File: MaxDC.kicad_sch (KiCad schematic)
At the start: 32 parts, among them J1 Screw_Terminal_01x03, J2 Screw_Terminal_01x04, T2 70063K

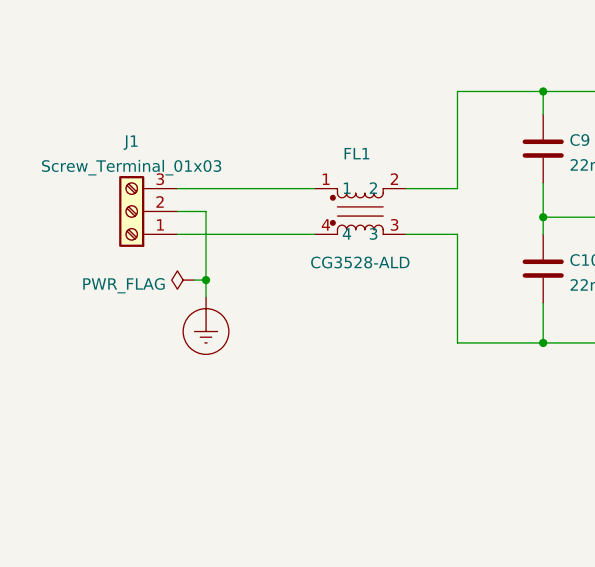
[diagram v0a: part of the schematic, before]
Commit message: Add files via upload
Begin Changes for creepage.   Reverse N and E input terminals.
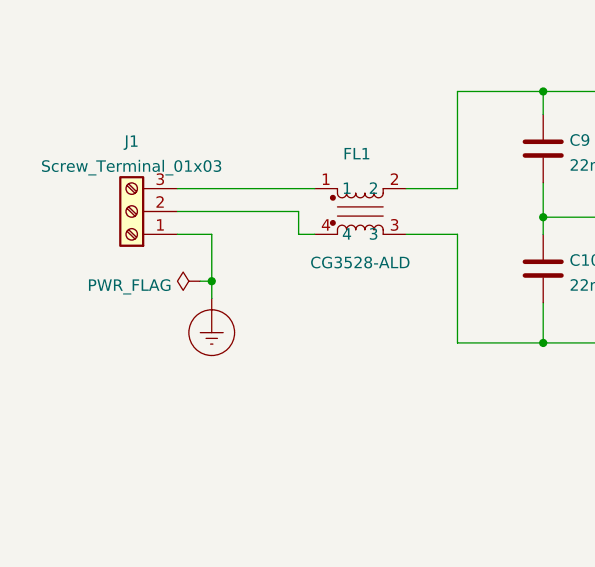
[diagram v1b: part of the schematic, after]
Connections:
- net Earth_Protective: now also J1.1 (Pin_1); no longer J1.2 (Pin_2)
- net at FL1.4: now also J1.2 (Pin_2); no longer J1.1 (Pin_1)
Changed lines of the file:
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@@
   (junction (at 164.465 110.49) (diameter 0) (color 0 0 0 0)
   )
-  (junction (at 45.085 92.71) (diameter 0) (color 0 0 0 0)
-  )
   (junction (at 134.62 110.49) (diameter 0) (color 0 0 0 0)
   )
@@
   (junction (at 82.55 85.725) (diameter 0) (color 0 0 0 0)
   )
+  (junction (at 45.72 92.837) (diameter 0) (color 0 0 0 0)
+  )
   (junction (at 200.66 60.325) (diameter 0) (color 0 0 0 0)
   )
@@
     (stroke (width 0) (type default) (color 0 0 0 0))
   )
+  (wire (pts (xy 45.72 92.837) (xy 45.72 94.742))
+    (stroke (width 0) (type default) (color 0 0 0 0))
+  )
   (wire (pts (xy 130.81 41.275) (xy 130.81 43.815))
     (stroke (width 0) (type default) (color 0 0 0 0))
@@
     (stroke (width 0) (type default) (color 0 0 0 0))
   )
-  (wire (pts (xy 45.085 92.71) (xy 45.085 85.09))
-    (stroke (width 0) (type default) (color 0 0 0 0))
-  )
   (wire (pts (xy 245.745 67.945) (xy 251.46 67.945))
     (stroke (width 0) (type default) (color 0 0 0 0))
@@
     (stroke (width 0) (type default) (color 0 0 0 0))
   )
-  (wire (pts (xy 45.085 92.71) (xy 45.085 94.615))
+  (wire (pts (xy 55.372 87.63) (xy 57.15 87.63))
     (stroke (width 0) (type default) (color 0 0 0 0))
   )
@@
     (stroke (width 0) (type default) (color 0 0 0 0))
   )
+  (wire (pts (xy 41.91 87.63) (xy 45.72 87.63))
+    (stroke (width 0) (type default) (color 0 0 0 0))
+  )
   (wire (pts (xy 164.465 86.36) (xy 179.07 86.36))
     (stroke (width 0) (type default) (color 0 0 0 0))
@@
     (stroke (width 0) (type default) (color 0 0 0 0))
   )
-  (wire (pts (xy 41.91 85.09) (xy 45.085 85.09))
-    (stroke (width 0) (type default) (color 0 0 0 0))
-  )
   (wire (pts (xy 148.59 86.36) (xy 148.59 92.075))
     (stroke (width 0) (type default) (color 0 0 0 0))
@@
     (stroke (width 0) (type default) (color 0 0 0 0))
   )
+  (wire (pts (xy 41.91 85.09) (xy 55.372 85.09))
+    (stroke (width 0) (type default) (color 0 0 0 0))
+  )
   (wire (pts (xy 156.21 59.055) (xy 156.21 60.325))
     (stroke (width 0) (type default) (color 0 0 0 0))
@@
     (stroke (width 0) (type default) (color 0 0 0 0))
   )
+  (wire (pts (xy 55.372 85.09) (xy 55.372 87.63))
+    (stroke (width 0) (type default) (color 0 0 0 0))
+  )
   (wire (pts (xy 73.025 82.55) (xy 73.025 71.755))
     (stroke (width 0) (type default) (color 0 0 0 0))
@@
     (stroke (width 0) (type default) (color 0 0 0 0))
   )
+  (wire (pts (xy 45.72 87.63) (xy 45.72 92.837))
+    (stroke (width 0) (type default) (color 0 0 0 0))
+  )
   (wire (pts (xy 245.745 70.485) (xy 251.46 70.485))
     (stroke (width 0) (type default) (color 0 0 0 0))
@@
     (stroke (width 0) (type default) (color 0 0 0 0))
   )
-  (wire (pts (xy 41.91 87.63) (xy 57.15 87.63))
-    (stroke (width 0) (type default) (color 0 0 0 0))
-  )
-  (wire (pts (xy 43.815 92.71) (xy 45.085 92.71))
+  (wire (pts (xy 44.45 92.837) (xy 45.72 92.837))
     (stroke (width 0) (type default) (color 0 0 0 0))
   )
@@
     (pin "2")
   )
-  (symbol (lib_id "power:Earth_Protective") (at 45.085 94.615 0) (unit 1)
+  (symbol (lib_id "power:Earth_Protective") (at 45.72 94.742 0) (unit 1)
     (in_bom yes) (on_board yes) (fields_autoplaced)
-    (property "Reference" "#PWR0101" (id 0) (at 51.435 100.965 0)
-      (effects (font (size 1.27 1.27)) hide)
-    )
-    (property "Value" "Earth_Protective" (id 1) (at 56.515 98.425 0)
-      (effects (font (size 1.27 1.27)) hide)
-    )
-    (property "Footprint" "" (id 2) (at 45.085 97.155 0)
-      (effects (font (size 1.27 1.27)) hide)
-    )
-    (property "Datasheet" "~" (id 3) (at 45.085 97.155 0)
+    (property "Reference" "#PWR0101" (id 0) (at 52.07 101.092 0)
+      (effects (font (size 1.27 1.27)) hide)
+    )
+    (property "Value" "Earth_Protective" (id 1) (at 57.15 98.552 0)
+      (effects (font (size 1.27 1.27)) hide)
+    )
+    (property "Footprint" "" (id 2) (at 45.72 97.282 0)
+      (effects (font (size 1.27 1.27)) hide)
+    )
+    (property "Datasheet" "~" (id 3) (at 45.72 97.282 0)
       (effects (font (size 1.27 1.27)) hide)
     )
@@
     )
   )
-  (symbol (lib_id "power:PWR_FLAG") (at 43.815 92.71 90) (unit 1)
+  (symbol (lib_id "power:PWR_FLAG") (at 44.45 92.837 90) (unit 1)
     (in_bom yes) (on_board yes) (fields_autoplaced)
-    (property "Reference" "#FLG0101" (id 0) (at 41.91 92.71 0)
-      (effects (font (size 1.27 1.27)) hide)
-    )
-    (property "Value" "PWR_FLAG" (id 1) (at 40.6401 93.189 90)
+    (property "Reference" "#FLG0101" (id 0) (at 42.545 92.837 0)
+      (effects (font (size 1.27 1.27)) hide)
+    )
+    (property "Value" "PWR_FLAG" (id 1) (at 41.2751 93.316 90)
       (effects (font (size 1.27 1.27)) (justify left))
     )
-    (property "Footprint" "" (id 2) (at 43.815 92.71 0)
-      (effects (font (size 1.27 1.27)) hide)
-    )
-    (property "Datasheet" "~" (id 3) (at 43.815 92.71 0)
-      (effects (font (size 1.27 1.27)) hide)
-    )
+    (property "Footprint" "" (id 2) (at 44.45 92.837 0)
+      (effects (font (size 1.27 1.27)) hide)
+    )
+    (property "Datasheet" "~" (id 3) (at 44.45 92.837 0)
+      (effects (font (size 1.27 1.27)) hide)
+    )

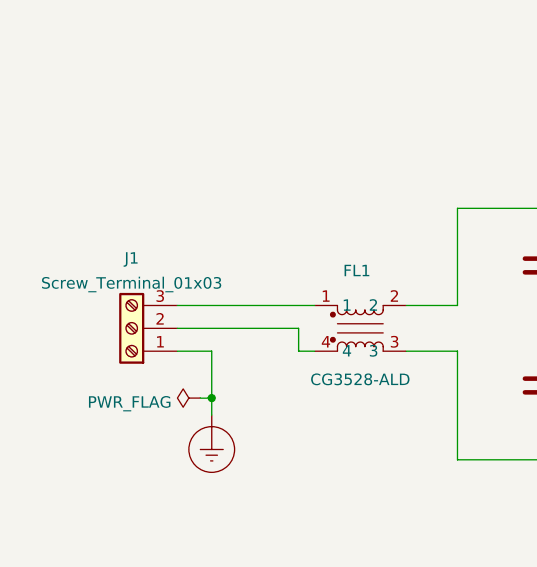
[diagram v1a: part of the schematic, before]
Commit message: Add files via upload
Adjust placement and spacing for 240VAC safety.   Slots not needed.
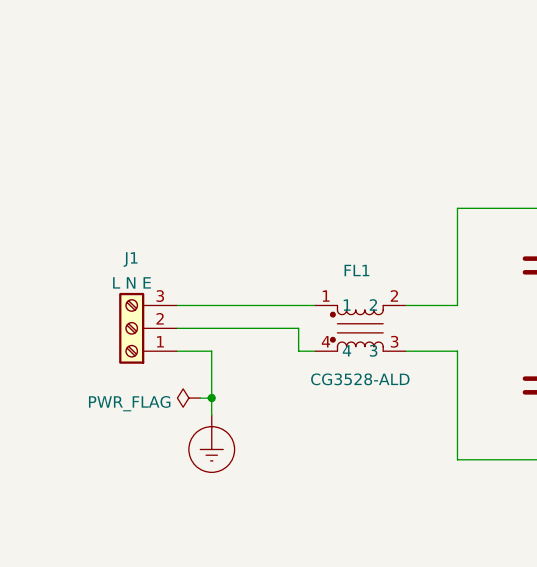
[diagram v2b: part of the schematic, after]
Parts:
- C10, C9: footprint Capacitor_THT:C_Rect_L18.0mm_W7.0mm_P15.00mm_FKS3_FKP3 -> Capacitor_THT:C_Rect_L18.0mm_W8.0mm_P15.00mm_FKS3_FKP3
- J1: value Screw_Terminal_01x03 -> L N E
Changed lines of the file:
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@@
   (title_block
     (title "MaxDC")
-    (date "2023-01-23")
+    (date "2023-01-24")
     (rev "0.2")
     (company "Author: Andrew Fischer\\nLicense: CC BY-NC 4.0 \\ncreativecommons.org/licenses/by-nc/4.0")
@@
     (in_bom yes) (on_board yes) (fields_autoplaced)
     (property "Reference" "J1" (id 0) (at 36.83 77.3135 0))
-    (property "Value" "Screw_Terminal_01x03" (id 1) (at 36.83 80.0886 0))
+    (property "Value" "L N E" (id 1) (at 36.83 80.0886 0))
     (property "Footprint" "TerminalBlock_Phoenix:TerminalBlock_Phoenix_MKDS-3-3-5.08_1x03_P5.08mm_Horizontal" (id 2) (at 36.83 85.09 0)
       (effects (font (size 1.27 1.27)) hide)
@@
       (effects (font (size 1.27 1.27)) (justify left))
     )
-    (property "Footprint" "Capacitor_THT:C_Rect_L18.0mm_W7.0mm_P15.00mm_FKS3_FKP3" (id 2) (at 83.5152 95.25 0)
+    (property "Footprint" "Capacitor_THT:C_Rect_L18.0mm_W8.0mm_P15.00mm_FKS3_FKP3" (id 2) (at 83.5152 95.25 0)
       (effects (font (size 1.27 1.27)) hide)
     )
@@
       (effects (font (size 1.27 1.27)) (justify left))
     )
-    (property "Footprint" "Capacitor_THT:C_Rect_L18.0mm_W7.0mm_P15.00mm_FKS3_FKP3" (id 2) (at 83.5152 81.915 0)
+    (property "Footprint" "Capacitor_THT:C_Rect_L18.0mm_W8.0mm_P15.00mm_FKS3_FKP3" (id 2) (at 83.5152 81.915 0)
       (effects (font (size 1.27 1.27)) hide)
     )
@@
     )
     (path "/f6f2e88a-815f-4070-b649-6d25db987473"
-      (reference "C9") (unit 1) (value "22nF") (footprint "Capacitor_THT:C_Rect_L18.0mm_W7.0mm_P15.00mm_FKS3_FKP3")
+      (reference "C9") (unit 1) (value "22nF") (footprint "Capacitor_THT:C_Rect_L18.0mm_W8.0mm_P15.00mm_FKS3_FKP3")
     )
     (path "/f46e4ec6-65a3-43ca-ba01-562772b6925d"
-      (reference "C10") (unit 1) (value "22nF") (footprint "Capacitor_THT:C_Rect_L18.0mm_W7.0mm_P15.00mm_FKS3_FKP3")
+      (reference "C10") (unit 1) (value "22nF") (footprint "Capacitor_THT:C_Rect_L18.0mm_W8.0mm_P15.00mm_FKS3_FKP3")
     )
     (path "/b1cd0cd8-a0ec-48c6-ae1d-c030f1e9f6c9"
@@
     )
     (path "/08e532fc-9580-46ad-af97-662135bee1de"
-      (reference "J1") (unit 1) (value "Screw_Terminal_01x03") (footprint "TerminalBlock_Phoenix:TerminalBlock_Phoenix_MKDS-3-3-5.08_1x03_P5.08mm_Horizontal")
+      (reference "J1") (unit 1) (value "L N E") (footprint "TerminalBlock_Phoenix:TerminalBlock_Phoenix_MKDS-3-3-5.08_1x03_P5.08mm_Horizontal")
     )
     (path "/c9494eea-a92e-41ee-83d6-7fde7a0d0d70"

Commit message: Add files via upload
28012023 Uploaded to JLCPCB
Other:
- note added: "C9 and C10 must be class Y."
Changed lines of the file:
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@@
   (title_block
     (title "MaxDC")
-    (date "2023-01-24")
-    (rev "0.2")
+    (date "2023-01-28")
+    (rev "0.3")
     (company "Author: Andrew Fischer\\nLicense: CC BY-NC 4.0 \\ncreativecommons.org/licenses/by-nc/4.0")
   )
@@
     (stroke (width 0) (type default) (color 0 0 0 0))
   )
+  (text "C9 and C10 must be class Y." (at 70.612 120.65 0)
+    (effects (font (size 2.54 2.54)) (justify left bottom))
+  )
   (global_label "T4" (shape input) (at 215.265 76.835 0) (fields_autoplaced)
